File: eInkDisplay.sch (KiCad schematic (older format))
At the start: 17 parts, among them J2901 FPC 1x24, Q2901 Q_PJFET_GDS

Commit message: Added PCA9745B16B. Updated schematic. ERC Passes.
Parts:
- J2901: symbol Connector_Generic:Conn_01x24 -> Macro_Keyboard:Conn_01x24
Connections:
- wire segments 47 -> 46
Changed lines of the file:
@@
 NoConn ~ 7800 2950
 $Comp
-L Connector_Generic:Conn_01x24 J2901
+L Macro_Keyboard:Conn_01x24 J2901
 U 1 1 61A8C93F
 P 8000 3750
@@
 U 1 1 61A8EEB3
 P 6000 2750
-F 0 "Q2901" H 5850 2650 50  0000 L CNN
+F 0 "Q2901" H 5750 2600 50  0000 L CNN
 F 1 "Q_PJFET_GDS" H 5500 2900 50  0000 L CNN
 F 2 "Package_TO_SOT_SMD:SOT-23" H 6200 2850 50  0001 C CNN
@@
 P 4850 3300
 F 0 "D2902" H 4900 3400 50  0000 R CNN
-F 1 "MBR0530" H 5050 3200 50  0000 R CNN
+F 1 "MBR0530" H 4850 3200 50  0000 R CNN
 F 2 "Diode_SMD:D_SOD-123" V 4850 3300 50  0001 C CNN
 F 3 "https://www.mccsemi.com/pdf/Products/MBR0520-MBR0580(SOD123).pdf" V 4850 3300 50  0001 C CNN
@@
 U 1 1 61A9411A
 P 5150 2850
-F 0 "D2903" H 5100 2900 50  0000 R CNN
-F 1 "MBR0530" H 5350 2750 50  0000 R CNN
+F 0 "D2903" H 5450 2900 50  0000 R CNN
+F 1 "MBR0530" H 5450 2750 50  0000 R CNN
 F 2 "Diode_SMD:D_SOD-123" V 5150 2850 50  0001 C CNN
 F 3 "https://www.mccsemi.com/pdf/Products/MBR0520-MBR0580(SOD123).pdf" V 5150 2850 50  0001 C CNN
@@
 U 1 1 61A94C59
 P 4850 2850
-F 0 "C2902" V 4750 2900 50  0000 L CNN
-F 1 "4.7 uF 10% 10V" V 4950 2700 50  0000 L CNN
+F 0 "C2902" V 4750 2750 50  0000 L CNN
+F 1 "4.7 uF 10% 10V" V 4950 2500 50  0000 L CNN
 F 2 "Capacitor_SMD:C_0805_2012Metric_Pad1.18x1.45mm_HandSolder" H 4850 2850 50  0001 C CNN
 F 3 "http://www.samsungsem.com/kr/support/product-search/mlcc/CL21A475KPFNNNE.jsp" H 4850 2850 50  0001 C CNN
@@
 U 1 1 61A91DEE
 P 5150 3300
-F 0 "C2903" V 5100 3350 50  0000 L CNN
-F 1 "1 uF 10% 10V" V 5250 3150 50  0000 L CNN
+F 0 "C2903" V 5100 3000 50  0000 L CNN
+F 1 "1 uF 10% 10V" V 5250 2950 50  0000 L CNN
 F 2 "Capacitor_SMD:C_0805_2012Metric_Pad1.18x1.45mm_HandSolder" H 5150 3300 50  0001 C CNN
 F 3 "http://www.samsungsem.com/kr/support/product-search/mlcc/CL21B105KPFNNNE.jsp" H 5150 3300 50  0001 C CNN
@@
 Wire Wire Line
 	5150 3050 5550 3050
-Wire Wire Line
-	5550 3100 5550 4650
-Wire Wire Line
-	5550 4650 7800 4650
 Connection ~ 5150 3050
 Wire Wire Line
@@
 U 1 1 61A9D08F
 P 5750 4150
-F 0 "C2904" V 5700 4200 50  0000 L CNN
+F 0 "C2904" V 5650 4100 50  0000 L CNN
 F 1 "1 uF 10% 10V" V 5850 4000 50  0000 L CNN
 F 2 "Capacitor_SMD:C_0805_2012Metric_Pad1.18x1.45mm_HandSolder" H 5750 4150 50  0001 C CNN
@@
 F 6 "CL21B105KPFNNNE" H 7400 4550 50  0001 C CNN "MFG #"
 	1    7400 4550
-	0    -1   -1   0
-$EndComp
-$Comp
-L power:GND #PWR02906
-U 1 1 61AA5BFE
-P 6950 4550
-F 0 "#PWR02906" H 6950 4300 50  0001 C CNN
-F 1 "GND" V 6955 4422 50  0000 R CNN
-F 2 "" H 6950 4550 50  0001 C CNN
-F 3 "" H 6950 4550 50  0001 C CNN
-	1    6950 4550
-	0    1    1    0
-$EndComp
-Wire Wire Line
-	6950 4550 7300 4550
-Wire Wire Line
-	7500 4550 7800 4550
+	0    1    1    0
+$EndComp
 $Comp
 L Device:C_Small C2908
@@
 Wire Wire Line
 	7800 3550 6600 3550
+Wire Wire Line
+	5550 3050 5550 4650
+Wire Wire Line
+	7500 4550 7800 4550
+Wire Wire Line
+	5550 4650 7800 4650
+$Comp
+L power:GND #PWR0111
+U 1 1 61A37FEC
+P 7300 4550
+F 0 "#PWR0111" H 7300 4300 50  0001 C CNN
+F 1 "GND" V 7305 4422 50  0000 R CNN
+F 2 "" H 7300 4550 50  0001 C CNN
+F 3 "" H 7300 4550 50  0001 C CNN
+	1    7300 4550
+	0    1    1    0
+$EndComp
 $EndSCHEMATC

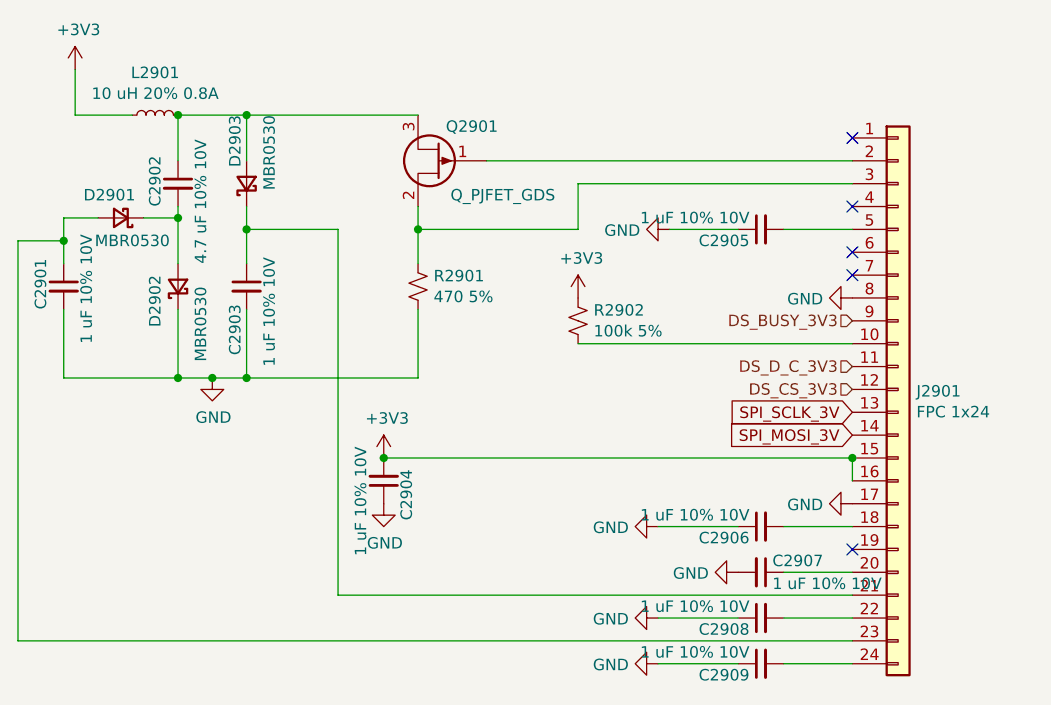
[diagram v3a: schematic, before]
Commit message: Layout completed. Design check passes.
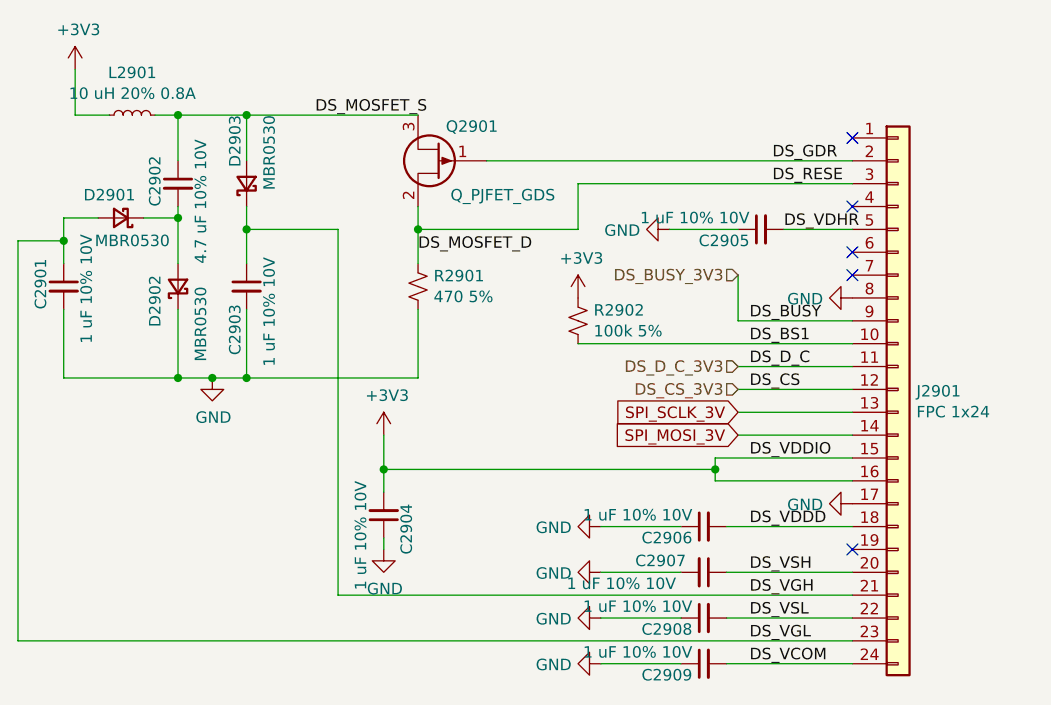
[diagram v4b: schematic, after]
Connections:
- net DS_BS1: now reaches J2901.10 (Pin_10), R2902.2
- net DS_VDDD: now reaches C2906.2, J2901.18 (Pin_18)
- net DS_GDR: now reaches J2901.2 (Pin_2), Q2901.1 (G)
- net DS_VSH: now reaches C2907.1, J2901.20 (Pin_20)
- net DS_VGH: now reaches C2903.1, D2903.1 (K), J2901.21 (Pin_21)
- net DS_VSL: now reaches C2908.2, J2901.22 (Pin_22)
- net DS_VGL: now reaches C2901.1, D2901.2 (A), J2901.23 (Pin_23)
- net DS_VCOM: now reaches C2909.2, J2901.24 (Pin_24)
- net DS_MOSFET_D: now reaches J2901.3 (Pin_3), Q2901.2 (D), R2901.1
- net DS_VDHR: now reaches C2905.2, J2901.5 (Pin_5)
- net DS_MOSFET_S: now reaches C2902.1, D2903.2 (A), L2901.2, Q2901.3 (S)
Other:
- moved on the sheet: C2904, C2906, C2907, C2908, C2909, L2901

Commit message: Change J2901 to Amphenon connector
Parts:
- J2901: footprint Macro Keyboard:Molex_502244_1x24_FPC -> Macro Keyboard:Amphenol_F31L-1A7H1-11024
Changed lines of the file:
@@
 F 0 "J2901" H 8080 3742 50  0000 L CNN
 F 1 "FPC 1x24" H 8080 3651 50  0000 L CNN
-F 2 "Macro Keyboard:Molex_502244_1x24_FPC" H 8000 3750 50  0001 C CNN
+F 2 "Macro Keyboard:Amphenol_F31L-1A7H1-11024" H 8000 3750 50  0001 C CNN
 F 3 "https://www.molex.com/pdm_docs/sd/5052782433_sd.pdf" H 8000 3750 50  0001 C CNN
 F 4 "WM20872CT-ND" H 8000 3750 50  0001 C CNN "Digikey PN"

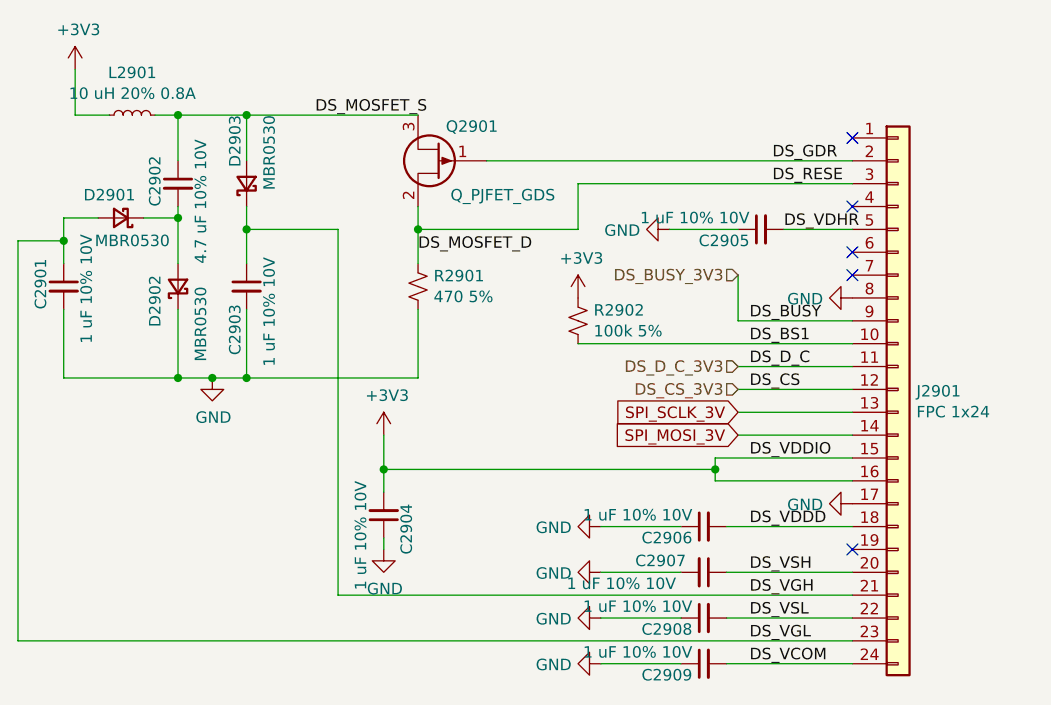
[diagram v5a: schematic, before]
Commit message: Fix design error in PI4ULS5V201TAEX. Reset and reassigned all annotations.
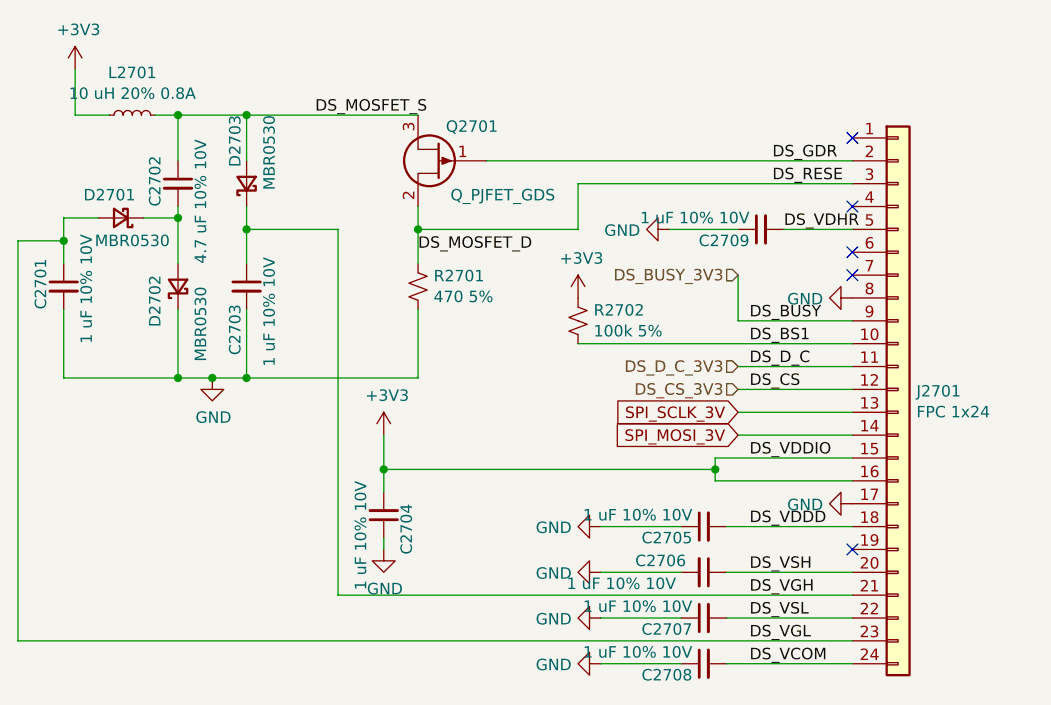
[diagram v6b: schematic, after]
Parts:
- renumbered C2901 to C2701, C2902 to C2702, C2903 to C2703, C2904 to C2704, C2906 to C2705, C2907 to C2706, C2908 to C2707, C2909 to C2708, C2905 to C2709, D2901 to D2701, D2902 to D2702, D2903 to D2703, J2901 to J2701, L2901 to L2701, Q2901 to Q2701, R2901 to R2701, R2902 to R2702
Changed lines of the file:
@@
 NoConn ~ 7800 2950
 $Comp
-L Macro_Keyboard:Conn_01x24 J2901
+L Macro_Keyboard:Conn_01x24 J2701
 U 1 1 61A8C93F
 P 8000 3750
-F 0 "J2901" H 8080 3742 50  0000 L CNN
+F 0 "J2701" H 8080 3742 50  0000 L CNN
 F 1 "FPC 1x24" H 8080 3651 50  0000 L CNN
 F 2 "Macro Keyboard:Amphenol_F31L-1A7H1-11024" H 8000 3750 50  0001 C CNN
@@
 NoConn ~ 7800 4450
 $Comp
-L Device:Q_PJFET_GDS Q2901
+L Device:Q_PJFET_GDS Q2701
 U 1 1 61A8EEB3
 P 6000 2750
-F 0 "Q2901" H 5750 2600 50  0000 L CNN
+F 0 "Q2701" H 5750 2600 50  0000 L CNN
 F 1 "Q_PJFET_GDS" H 5500 2900 50  0000 L CNN
 F 2 "Package_TO_SOT_SMD:SOT-23" H 6200 2850 50  0001 C CNN
@@
 	7800 2750 6200 2750
 $Comp
-L Device:L_Small L2901
+L Device:L_Small L2701
 U 1 1 61A90080
 P 4650 2550
-F 0 "L2901" V 4835 2550 50  0000 C CNN
+F 0 "L2701" V 4835 2550 50  0000 C CNN
 F 1 "10 uH 20% 0.8A" V 4744 2550 50  0000 C CNN
 F 2 "Inductor_SMD:L_Taiyo-Yuden_NR-40xx_HandSoldering" H 4650 2550 50  0001 C CNN
@@
 $EndComp
 $Comp
-L power:+3V3 #PWR02901
+L power:+3V3 #PWR02701
 U 1 1 61A90F00
 P 4400 2350
-F 0 "#PWR02901" H 4400 2200 50  0001 C CNN
+F 0 "#PWR02701" H 4400 2200 50  0001 C CNN
 F 1 "+3V3" H 4415 2523 50  0000 C CNN
 F 2 "" H 4400 2350 50  0001 C CNN
@@
 	4850 2550 5150 2550
 $Comp
-L Device:R_Small_US R2901
+L Device:R_Small_US R2701
 U 1 1 61A9164C
 P 5900 3300
-F 0 "R2901" H 5968 3346 50  0000 L CNN
+F 0 "R2701" H 5968 3346 50  0000 L CNN
 F 1 "470 5%" H 5968 3255 50  0000 L CNN
 F 2 "Resistor_SMD:R_0805_2012Metric_Pad1.20x1.40mm_HandSolder" H 5900 3300 50  0001 C CNN
@@
 $EndComp
 $Comp
-L Device:C_Small C2901
+L Device:C_Small C2701
 U 1 1 61A9221A
 P 4350 3300
-F 0 "C2901" V 4250 3200 50  0000 L CNN
+F 0 "C2701" V 4250 3200 50  0000 L CNN
 F 1 "1 uF 10% 10V" V 4450 3050 50  0000 L CNN
 F 2 "Capacitor_SMD:C_0805_2012Metric_Pad1.18x1.45mm_HandSolder" H 4350 3300 50  0001 C CNN
@@
 $EndComp
 $Comp
-L Device:D_Schottky_Small D2902
+L Device:D_Schottky_Small D2702
 U 1 1 61A93B5D
 P 4850 3300
-F 0 "D2902" H 4900 3400 50  0000 R CNN
+F 0 "D2702" H 4900 3400 50  0000 R CNN
 F 1 "MBR0530" H 4850 3200 50  0000 R CNN
 F 2 "Diode_SMD:D_SOD-123" V 4850 3300 50  0001 C CNN
@@
 $EndComp
 $Comp
-L Device:D_Schottky_Small D2903
+L Device:D_Schottky_Small D2703
 U 1 1 61A9411A
 P 5150 2850
-F 0 "D2903" H 5450 2900 50  0000 R CNN
+F 0 "D2703" H 5450 2900 50  0000 R CNN
 F 1 "MBR0530" H 5450 2750 50  0000 R CNN
 F 2 "Diode_SMD:D_SOD-123" V 5150 2850 50  0001 C CNN
@@
 $EndComp
 $Comp
-L Device:D_Schottky_Small D2901
+L Device:D_Schottky_Small D2701
 U 1 1 61A94531
 P 4600 3000
-F 0 "D2901" H 4650 2900 50  0000 C CNN
+F 0 "D2701" H 4650 2900 50  0000 C CNN
 F 1 "MBR0530" H 4550 3100 50  0000 C CNN
 F 2 "Diode_SMD:D_SOD-123" V 4600 3000 50  0001 C CNN
@@
 $EndComp
 $Comp
-L Device:C_Small C2902
+L Device:C_Small C2702
 U 1 1 61A94C59
 P 4850 2850
-F 0 "C2902" V 4750 2750 50  0000 L CNN
+F 0 "C2702" V 4750 2750 50  0000 L CNN
 F 1 "4.7 uF 10% 10V" V 4950 2500 50  0000 L CNN
 F 2 "Capacitor_SMD:C_0805_2012Metric_Pad1.18x1.45mm_HandSolder" H 4850 2850 50  0001 C CNN
@@
 	4850 3700 5000 3700
 $Comp
-L Device:C_Small C2903
+L Device:C_Small C2703
 U 1 1 61A91DEE
 P 5150 3300
-F 0 "C2903" V 5100 3000 50  0000 L CNN
+F 0 "C2703" V 5100 3000 50  0000 L CNN
 F 1 "1 uF 10% 10V" V 5250 2950 50  0000 L CNN
 F 2 "Capacitor_SMD:C_0805_2012Metric_Pad1.18x1.45mm_HandSolder" H 5150 3300 50  0001 C CNN
@@
 $EndComp
 $Comp
-L power:GND #PWR02902
+L power:GND #PWR02702
 U 1 1 61A98858
 P 5000 3700
-F 0 "#PWR02902" H 5000 3450 50  0001 C CNN
+F 0 "#PWR02702" H 5000 3450 50  0001 C CNN
 F 1 "GND" H 5005 3527 50  0000 C CNN
 F 2 "" H 5000 3700 50  0001 C CNN
@@
 	4350 3100 4350 3000
 $Comp
-L power:+3V3 #PWR02903
+L power:+3V3 #PWR02703
 U 1 1 61A9BE75
 P 5750 3950
-F 0 "#PWR02903" H 5750 3800 50  0001 C CNN
+F 0 "#PWR02703" H 5750 3800 50  0001 C CNN
 F 1 "+3V3" H 5765 4123 50  0000 C CNN
 F 2 "" H 5750 3950 50  0001 C CNN
@@
 $EndComp
 $Comp
-L Device:C_Small C2904
+L Device:C_Small C2704
 U 1 1 61A9D08F
 P 5750 4300
-F 0 "C2904" V 5650 4250 50  0000 L CNN
+F 0 "C2704" V 5650 4250 50  0000 L CNN
 F 1 "1 uF 10% 10V" V 5850 4150 50  0000 L CNN
 F 2 "Capacitor_SMD:C_0805_2012Metric_Pad1.18x1.45mm_HandSolder" H 5750 4300 50  0001 C CNN
@@
 $EndComp
 $Comp
-L power:GND #PWR02904
+L power:GND #PWR02704
 U 1 1 61A9DB32
 P 5750 4450
-F 0 "#PWR02904" H 5750 4200 50  0001 C CNN
+F 0 "#PWR02704" H 5750 4200 50  0001 C CNN
 F 1 "GND" H 5755 4277 50  0000 C CNN
 F 2 "" H 5750 4450 50  0001 C CNN
@@
 $EndComp
 $Comp
-L Device:C_Small C2906
+L Device:C_Small C2705
 U 1 1 61AA1E17
 P 7150 4350
-F 0 "C2906" V 7100 4400 50  0000 L CNN
+F 0 "C2705" V 7100 4400 50  0000 L CNN
 F 1 "1 uF 10% 10V" V 7200 4400 50  0000 L CNN
 F 2 "Capacitor_SMD:C_0805_2012Metric_Pad1.18x1.45mm_HandSolder" H 7150 4350 50  0001 C CNN
@@
 $EndComp
 $Comp
-L power:GND #PWR02912
+L power:GND #PWR02712
 U 1 1 61AA39D4
 P 7800 4250
-F 0 "#PWR02912" H 7800 4000 50  0001 C CNN
+F 0 "#PWR02712" H 7800 4000 50  0001 C CNN
 F 1 "GND" V 7805 4122 50  0000 R CNN
 F 2 "" H 7800 4250 50  0001 C CNN
@@
 $EndComp
 $Comp
-L power:GND #PWR02906
+L power:GND #PWR02706
 U 1 1 61AA48B6
 P 6700 4350
-F 0 "#PWR02906" H 6700 4100 50  0001 C CNN
+F 0 "#PWR02706" H 6700 4100 50  0001 C CNN
 F 1 "GND" V 6705 4222 50  0000 R CNN
 F 2 "" H 6700 4350 50  0001 C CNN
@@
 	6700 4350 7050 4350
 $Comp
-L Device:C_Small C2907
+L Device:C_Small C2706
 U 1 1 61AA58CA
 P 7150 4550
-F 0 "C2907" V 7100 4250 50  0000 L CNN
+F 0 "C2706" V 7100 4250 50  0000 L CNN
 F 1 "1 uF 10% 10V" V 7200 3950 50  0000 L CNN
 F 2 "Capacitor_SMD:C_0805_2012Metric_Pad1.18x1.45mm_HandSolder" H 7150 4550 50  0001 C CNN
@@
 $EndComp
 $Comp
-L Device:C_Small C2905
+L Device:C_Small C2709
 U 1 1 61AAAB7A
 P 7400 3050
-F 0 "C2905" V 7350 3100 50  0000 L CNN
+F 0 "C2709" V 7350 3100 50  0000 L CNN
 F 1 "1 uF 10% 10V" V 7450 3100 50  0000 L CNN
 F 2 "Capacitor_SMD:C_0805_2012Metric_Pad1.18x1.45mm_HandSolder" H 7400 3050 50  0001 C CNN
@@
 $EndComp
 $Comp
-L power:GND #PWR02909
+L power:GND #PWR02710
 U 1 1 61AAB511
 P 7000 3050
-F 0 "#PWR02909" H 7000 2800 50  0001 C CNN
+F 0 "#PWR02710" H 7000 2800 50  0001 C CNN
 F 1 "GND" V 7005 2922 50  0000 R CNN
 F 2 "" H 7000 3050 50  0001 C CNN
@@
 	7500 3050 7800 3050
 $Comp
-L power:GND #PWR02911
+L power:GND #PWR02711
 U 1 1 61AADB6B
 P 7800 3350
-F 0 "#PWR02911" H 7800 3100 50  0001 C CNN
+F 0 "#PWR02711" H 7800 3100 50  0001 C CNN
 F 1 "GND" V 7805 3222 50  0000 R CNN
 F 2 "" H 7800 3350 50  0001 C CNN
@@
 DS_BUSY_3V3
 $Comp
-L Device:R_Small_US R2902
+L Device:R_Small_US R2702
 U 1 1 61AC5FE7
 P 6600 3450
-F 0 "R2902" H 6668 3496 50  0000 L CNN
+F 0 "R2702" H 6668 3496 50  0000 L CNN
 F 1 "100k 5%" H 6668 3405 50  0000 L CNN
 F 2 "Resistor_SMD:R_0805_2012Metric_Pad1.20x1.40mm_HandSolder" H 6600 3450 50  0001 C CNN
@@
 $EndComp
 $Comp
-L power:+3V3 #PWR02905
+L power:+3V3 #PWR02705
 U 1 1 61AC62EF
 P 6600 3350
-F 0 "#PWR02905" H 6600 3200 50  0001 C CNN
+F 0 "#PWR02705" H 6600 3200 50  0001 C CNN
 F 1 "+3V3" H 6615 3523 50  0000 C CNN
 F 2 "" H 6600 3350 50  0001 C CNN
@@
 	5550 4650 7800 4650
 $Comp
-L power:GND #PWR02910
+L power:GND #PWR02707
 U 1 1 61A37FEC
 P 6700 4550
-F 0 "#PWR02910" H 6700 4300 50  0001 C CNN
+F 0 "#PWR02707" H 6700 4300 50  0001 C CNN
 F 1 "GND" V 6705 4422 50  0000 R CNN
 F 2 "" H 6700 4550 50  0001 C CNN
@@
 DS_VGH
 $Comp
-L Device:C_Small C2908
+L Device:C_Small C2707
 U 1 1 61AA7346
 P 7150 4750
-F 0 "C2908" V 7100 4800 50  0000 L CNN
+F 0 "C2707" V 7100 4800 50  0000 L CNN
 F 1 "1 uF 10% 10V" V 7200 4800 50  0000 L CNN
 F 2 "Capacitor_SMD:C_0805_2012Metric_Pad1.18x1.45mm_HandSolder" H 7150 4750 50  0001 C CNN
@@
 	6700 4750 7050 4750
 $Comp
-L power:GND #PWR02907
+L power:GND #PWR02708
 U 1 1 61AA7F23
 P 6700 4750
-F 0 "#PWR02907" H 6700 4500 50  0001 C CNN
+F 0 "#PWR02708" H 6700 4500 50  0001 C CNN
 F 1 "GND" V 6705 4622 50  0000 R CNN
 F 2 "" H 6700 4750 50  0001 C CNN
@@
 	7250 4750 7800 4750
 $Comp
-L Device:C_Small C2909
+L Device:C_Small C2708
 U 1 1 61AA8D03
 P 7150 4950
-F 0 "C2909" V 7100 5000 50  0000 L CNN
+F 0 "C2708" V 7100 5000 50  0000 L CNN
 F 1 "1 uF 10% 10V" V 7200 5000 50  0000 L CNN
 F 2 "Capacitor_SMD:C_0805_2012Metric_Pad1.18x1.45mm_HandSolder" H 7150 4950 50  0001 C CNN
@@
 $EndComp
 $Comp
-L power:GND #PWR02908
+L power:GND #PWR02709
 U 1 1 61AA9A69
 P 6700 4950
-F 0 "#PWR02908" H 6700 4700 50  0001 C CNN
+F 0 "#PWR02709" H 6700 4700 50  0001 C CNN
 F 1 "GND" V 6705 4822 50  0000 R CNN
 F 2 "" H 6700 4950 50  0001 C CNN

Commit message: R2701 should be 0.47 ohm...not 470 ohm
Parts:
- R2701: value 470 5% -> 0.47 5%
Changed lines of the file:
@@
 P 5900 3300
 F 0 "R2701" H 5968 3346 50  0000 L CNN
-F 1 "470 5%" H 5968 3255 50  0000 L CNN
+F 1 "0.47 5%" H 5968 3255 50  0000 L CNN
 F 2 "Resistor_SMD:R_0805_2012Metric_Pad1.20x1.40mm_HandSolder" H 5900 3300 50  0001 C CNN
 F 3 "https://www.seielect.com/catalog/sei-rmcf_rmcp.pdf" H 5900 3300 50  0001 C CNN

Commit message: Updated so that eink reset pin is shared with GP04. Not ideal, but should work.
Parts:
- removed R2702: 100k 5%, Resistor_SMD:R_0805_2012Metric_Pad1.20x1.40mm_HandSolder, symbol Device:R_Small_US
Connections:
- net DS_BS1 renamed DS_RESET#_3V3
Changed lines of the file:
@@
 Text HLabel 7300 3250 0    50   Input ~ 0
 DS_BUSY_3V3
-$Comp
-L Device:R_Small_US R2702
-U 1 1 61AC5FE7
-P 6600 3450
-F 0 "R2702" H 6668 3496 50  0000 L CNN
-F 1 "100k 5%" H 6668 3405 50  0000 L CNN
-F 2 "Resistor_SMD:R_0805_2012Metric_Pad1.20x1.40mm_HandSolder" H 6600 3450 50  0001 C CNN
-F 3 "https://www.seielect.com/catalog/sei-rmcf_rmcp.pdf" H 6600 3450 50  0001 C CNN
-F 4 "RMCF0805JT100KCT-ND" H 6600 3450 50  0001 C CNN "Digikey PN"
-F 5 "Stackpole Electronics Inc" H 6600 3450 50  0001 C CNN "MFG"
-F 6 "RMCF0805JT100K" H 6600 3450 50  0001 C CNN "MFG #"
-	1    6600 3450
-	1    0    0    -1
-$EndComp
-$Comp
-L power:+3V3 #PWR02705
-U 1 1 61AC62EF
-P 6600 3350
-F 0 "#PWR02705" H 6600 3200 50  0001 C CNN
-F 1 "+3V3" H 6615 3523 50  0000 C CNN
-F 2 "" H 6600 3350 50  0001 C CNN
-F 3 "" H 6600 3350 50  0001 C CNN
-	1    6600 3350
-	1    0    0    -1
-$EndComp
-Wire Wire Line
-	7800 3550 6600 3550
 Wire Wire Line
 	5550 3050 5550 4650
@@
 Wire Wire Line
 	4550 2550 4400 2550
+Text HLabel 7300 3550 0    50   Input ~ 0
+DS_RESET#_3V3
+Wire Wire Line
+	7800 3550 7300 3550
 $EndSCHEMATC
